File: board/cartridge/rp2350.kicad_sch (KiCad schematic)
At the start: 28 parts, among them J3 TC2030-NL, P1 Card Edge, U2 RP2350B, U4 W25Q128JVS, Y1 ABM8-272-T3

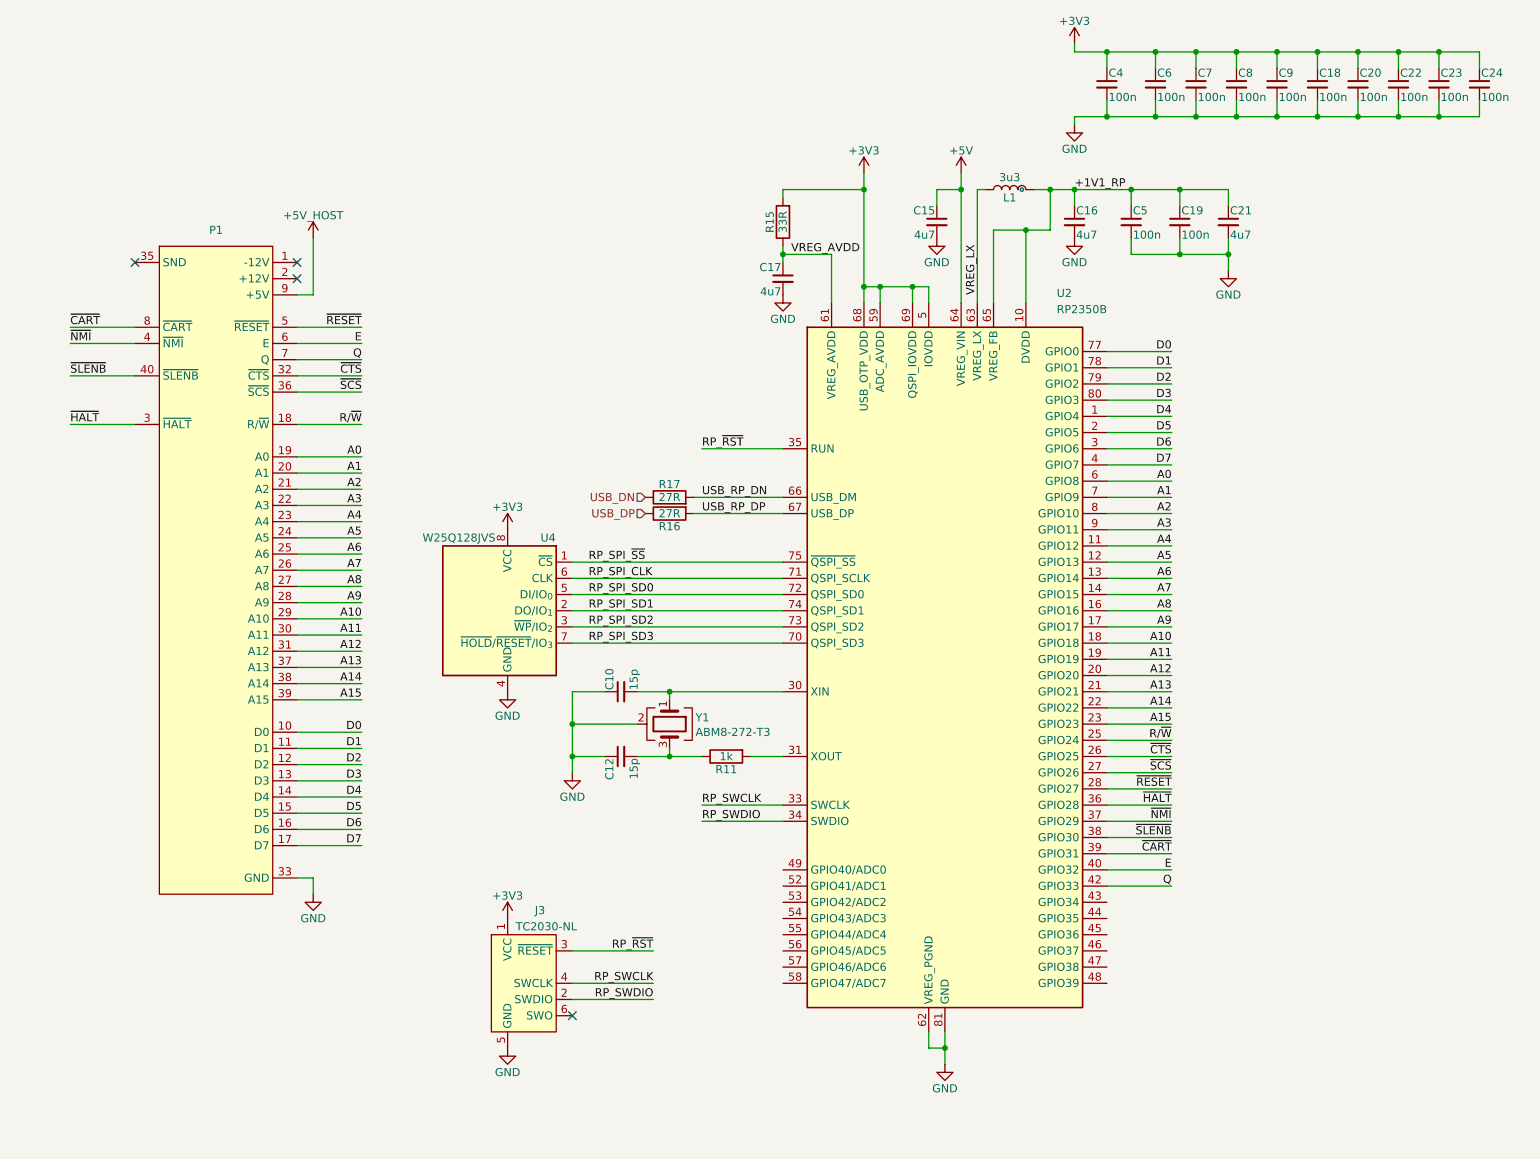
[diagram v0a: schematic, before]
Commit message: Finish routing RP2350.
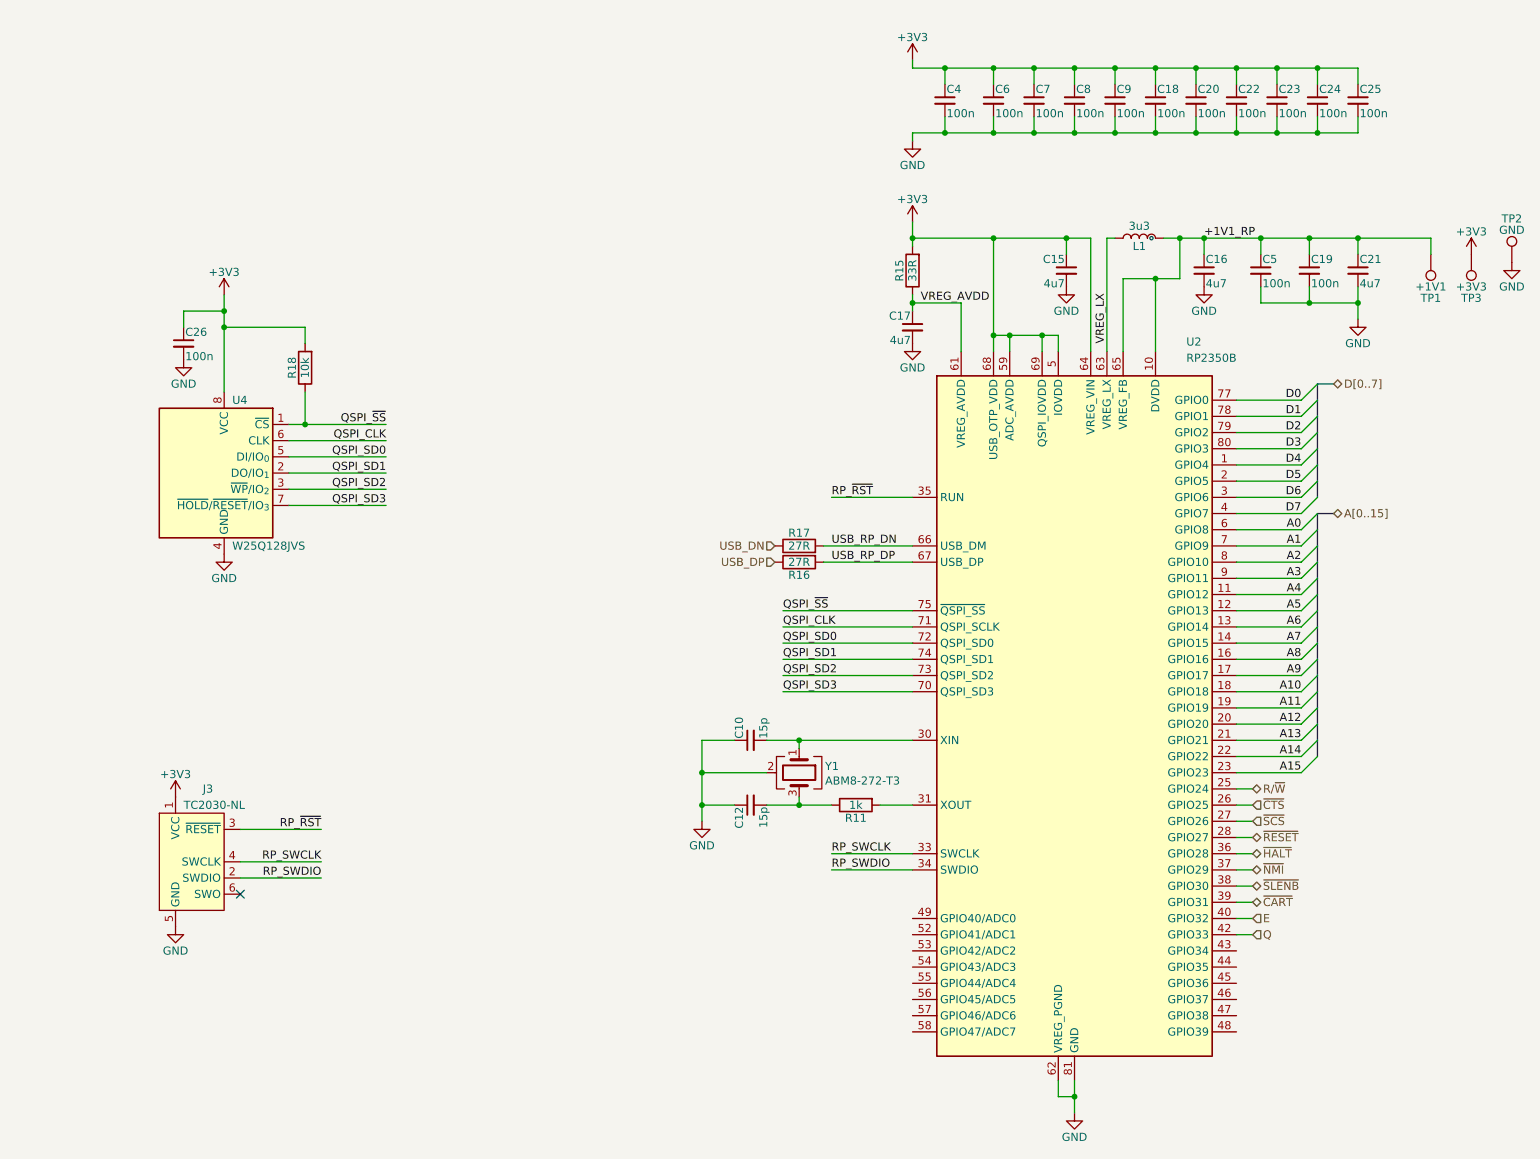
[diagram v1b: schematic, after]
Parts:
- removed P1: Card Edge, 0Project:CoCo_Cart, symbol 0Project:CoCo_Cart
- added C25, C26: 100n, Capacitor_SMD:C_0402_1005Metric, symbol Device:C_Small
- added R18: 10k, Resistor_SMD:R_0402_1005Metric, symbol Device:R
- added TP1: +1V1, TestPoint:TestPoint_Pad_D2.0mm, symbol Connector:TestPoint
- added TP2: GND, TestPoint:TestPoint_Pad_3.0x3.0mm, symbol Connector:TestPoint
- added TP3: +3V3, TestPoint:TestPoint_Pad_D2.0mm, symbol Connector:TestPoint
- U4: footprint Package_SO:SOIC-8_5.3x5.3mm_P1.27mm -> 0Project:SOIC-8_3.9-5.3x5.3mm_P1.27mm
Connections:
- net +5V is gone; now on net +3V3: C15.1, U2.64 (VREG_VIN)
- net +1V1_RP: now also TP1.1
- net +3V3: now also C25.1, C26.1, R18.2, TP3.1
- net GND: now also C25.2, C26.2, TP2.1
- net RP_SPI_CLK renamed QSPI_CLK
- net RP_SPI_SD0 renamed QSPI_SD0
- net RP_SPI_SD1 renamed QSPI_SD1
- net RP_SPI_SD2 renamed QSPI_SD2
- net RP_SPI_SD3 renamed QSPI_SD3
- net RP_SPI_~{SS} renamed QSPI_~{SS}
- net QSPI_~{SS}: now also R18.1
- no-connect marks 4 -> 1
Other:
- company: © 2023-2025 Sam Hanes, licensed CERN-OHL-W v2 -> © 2023-2026 Sam Hanes, licensed CERN-OHL-W v2
- moved on the sheet: C10, C12, C15, C16, C17, C18, C19, C20, C21, C22, C23, C24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

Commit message: Add RTC and start adding DAC.
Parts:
- added R27, R28: 1k, Resistor_SMD:R_0402_1005Metric, symbol Device:R
- TP2: footprint TestPoint:TestPoint_Pad_3.0x3.0mm -> TestPoint:TestPoint_Pad_4.0x4.0mm
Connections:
- net +3V3: now also R27.2, R28.2
- net SDA: now reaches U2.43 (GPIO34)
- net SDA: now also R27.1
- net SCL: now reaches U2.44 (GPIO35)
- net SCL: now also R28.1
- net SD_CLK: now reaches U2.53 (GPIO42/ADC2)
- net SD_CMD: now reaches U2.54 (GPIO43/ADC3)
- net SD_DAT0: now reaches U2.55 (GPIO44/ADC4)
- net SD_DAT1: now reaches U2.56 (GPIO45/ADC5)
- net SD_DAT2: now reaches U2.57 (GPIO46/ADC6)
- net SD_DAT3: now reaches U2.58 (GPIO47/ADC7)
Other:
- moved on the sheet: C26, J3, R18, U4

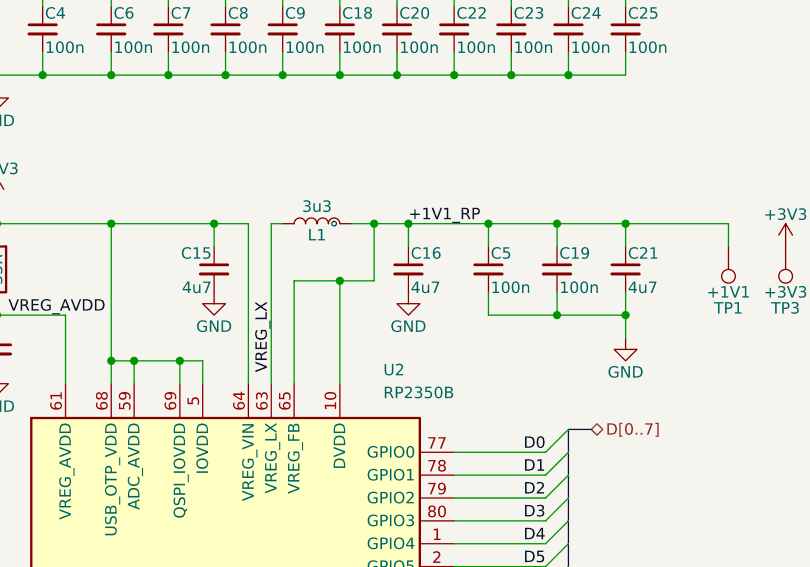
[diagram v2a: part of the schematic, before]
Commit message: Start playing with a test harness board.
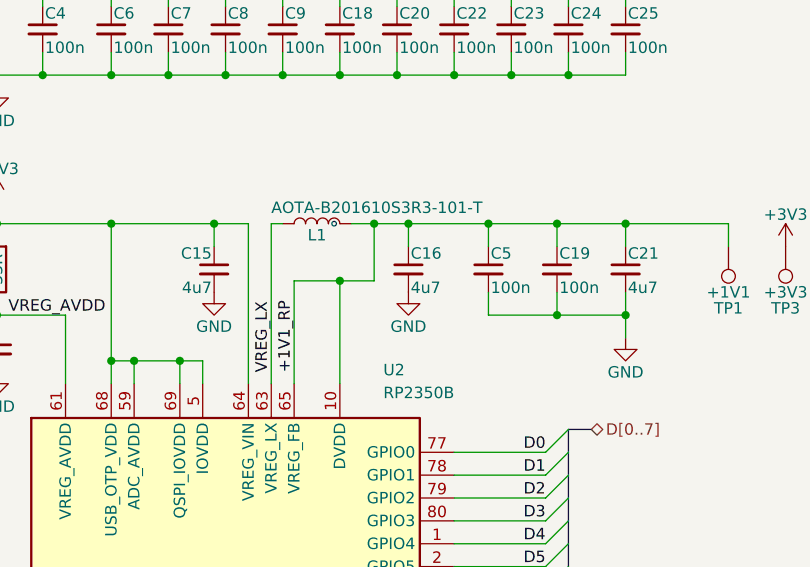
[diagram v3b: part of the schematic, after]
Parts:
- L1: value 3u3 -> AOTA-B201610S3R3-101-T; LCSC (none) -> C42411119
- U2: LCSC (none) -> C42415655
- Y1: LCSC (none) -> C20625731
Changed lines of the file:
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@@
 	)
 	(label "+1V1_RP"
-		(at 201.93 49.53 0)
+		(at 189.23 66.04 90)
 		(effects
 			(font
@@
 			)
 		)
-		(property "Value" "3u3"
-			(at 191.77 47.625 90)
+		(property "Value" "AOTA-B201610S3R3-101-T"
+			(at 186.69 47.752 90)
 			(effects
 				(font
 					(size 1.27 1.27)
 				)
+				(justify left)
 			)
 		)
@@
 			)
 		)
-		(property "Datasheet" "~"
+		(property "Datasheet" "https://abracon.com/datasheets/AOTA-B201610S3R3-101-T.pdf"
 			(at 191.77 49.53 0)
 			(effects
@@
 			)
 		)
+		(property "LCSC" "C42411119"
+			(at 191.77 49.53 90)
+			(effects
+				(font
+					(size 1.27 1.27)
+				)
+				(hide yes)
+			)
+		)
 		(pin "1"
 		)
@@
 			)
 		)
-		(property "Datasheet" "~"
+		(property "Datasheet" "https://abracon.com/datasheets/ABM8-272-T3.pdf"
 			(at 138.43 133.35 0)
 			(effects
@@
 			)
 		)
+		(property "LCSC" "C20625731"
+			(at 138.43 133.35 90)
+			(effects
+				(font
+					(size 1.27 1.27)
+				)
+				(hide yes)
+			)
+		)
 		(pin "4"
 		)
@@
 			(effects
 				(font
+					(size 1.27 1.27)
+				)
+				(hide yes)
+			)
+		)
+		(property "LCSC" "C42415655"
+			(at 181.61 123.19 0)
+			(effects
+				(font
